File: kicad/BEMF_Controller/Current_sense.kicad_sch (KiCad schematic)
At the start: 24 parts, among them U13 INA181, U14 INA181, U15 INA181, U2 INA181

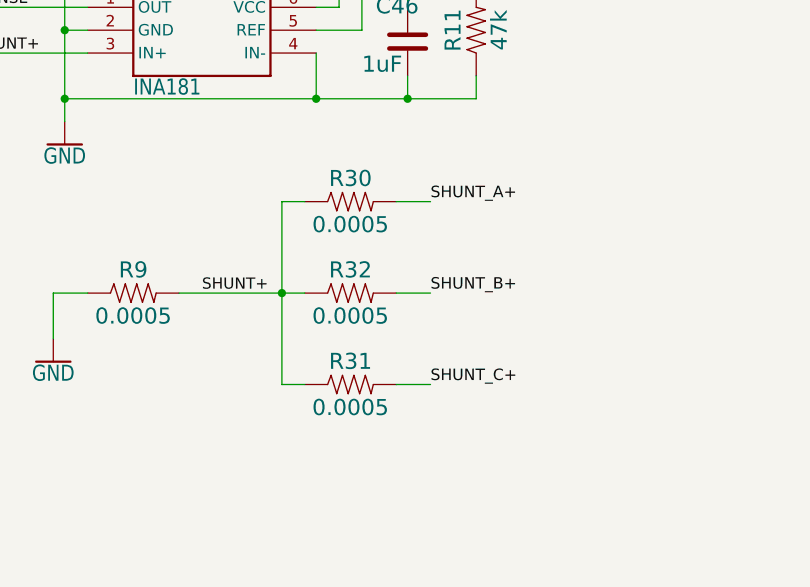
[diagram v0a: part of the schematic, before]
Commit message: Several updates to analog section
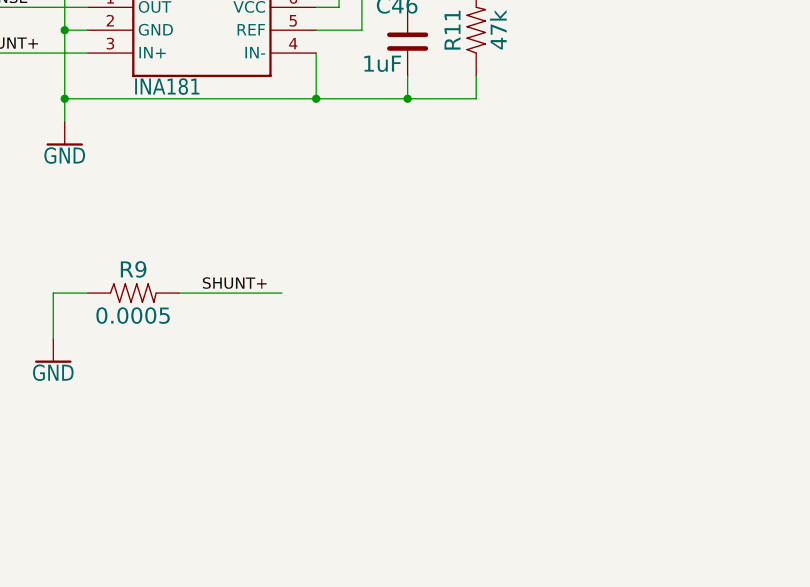
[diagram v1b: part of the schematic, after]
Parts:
- removed R30, R31, R32: 0.0005, main:R2512, symbol main-eagle-import:RESISTOR

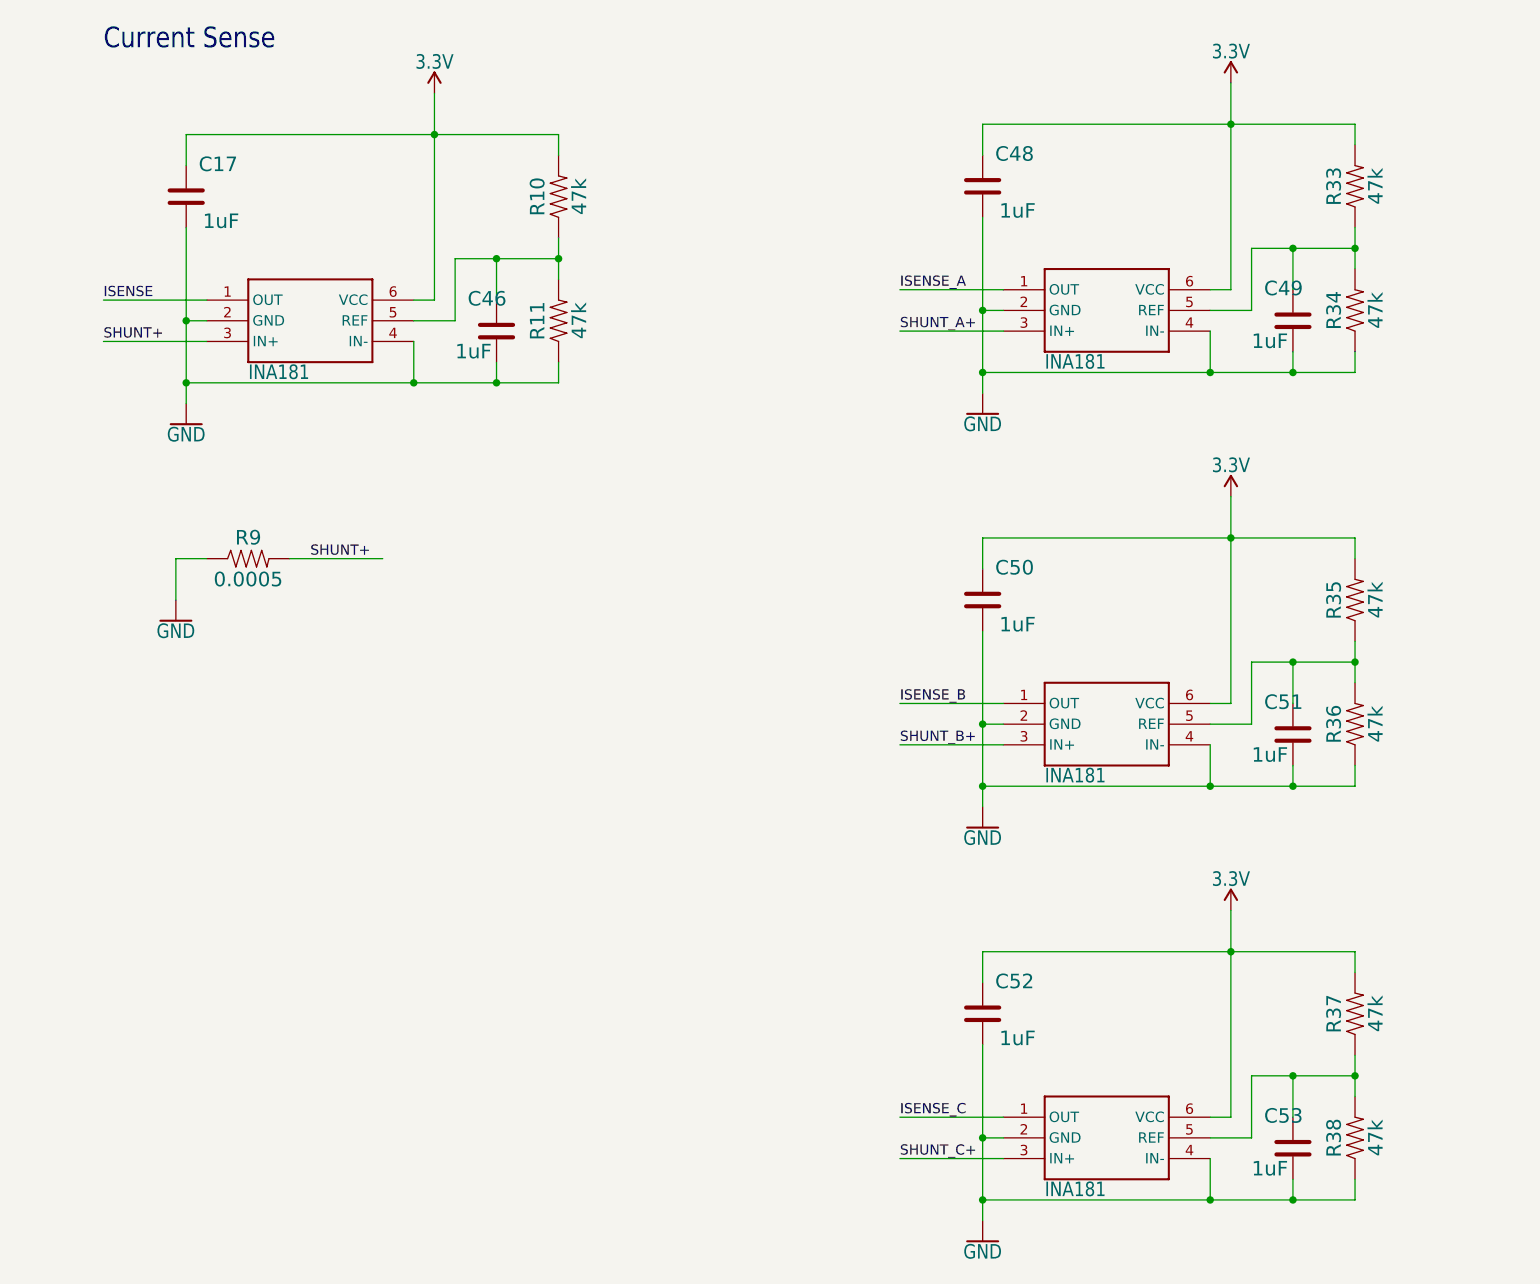
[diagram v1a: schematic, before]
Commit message: Further work on a/o current sensing circuits.
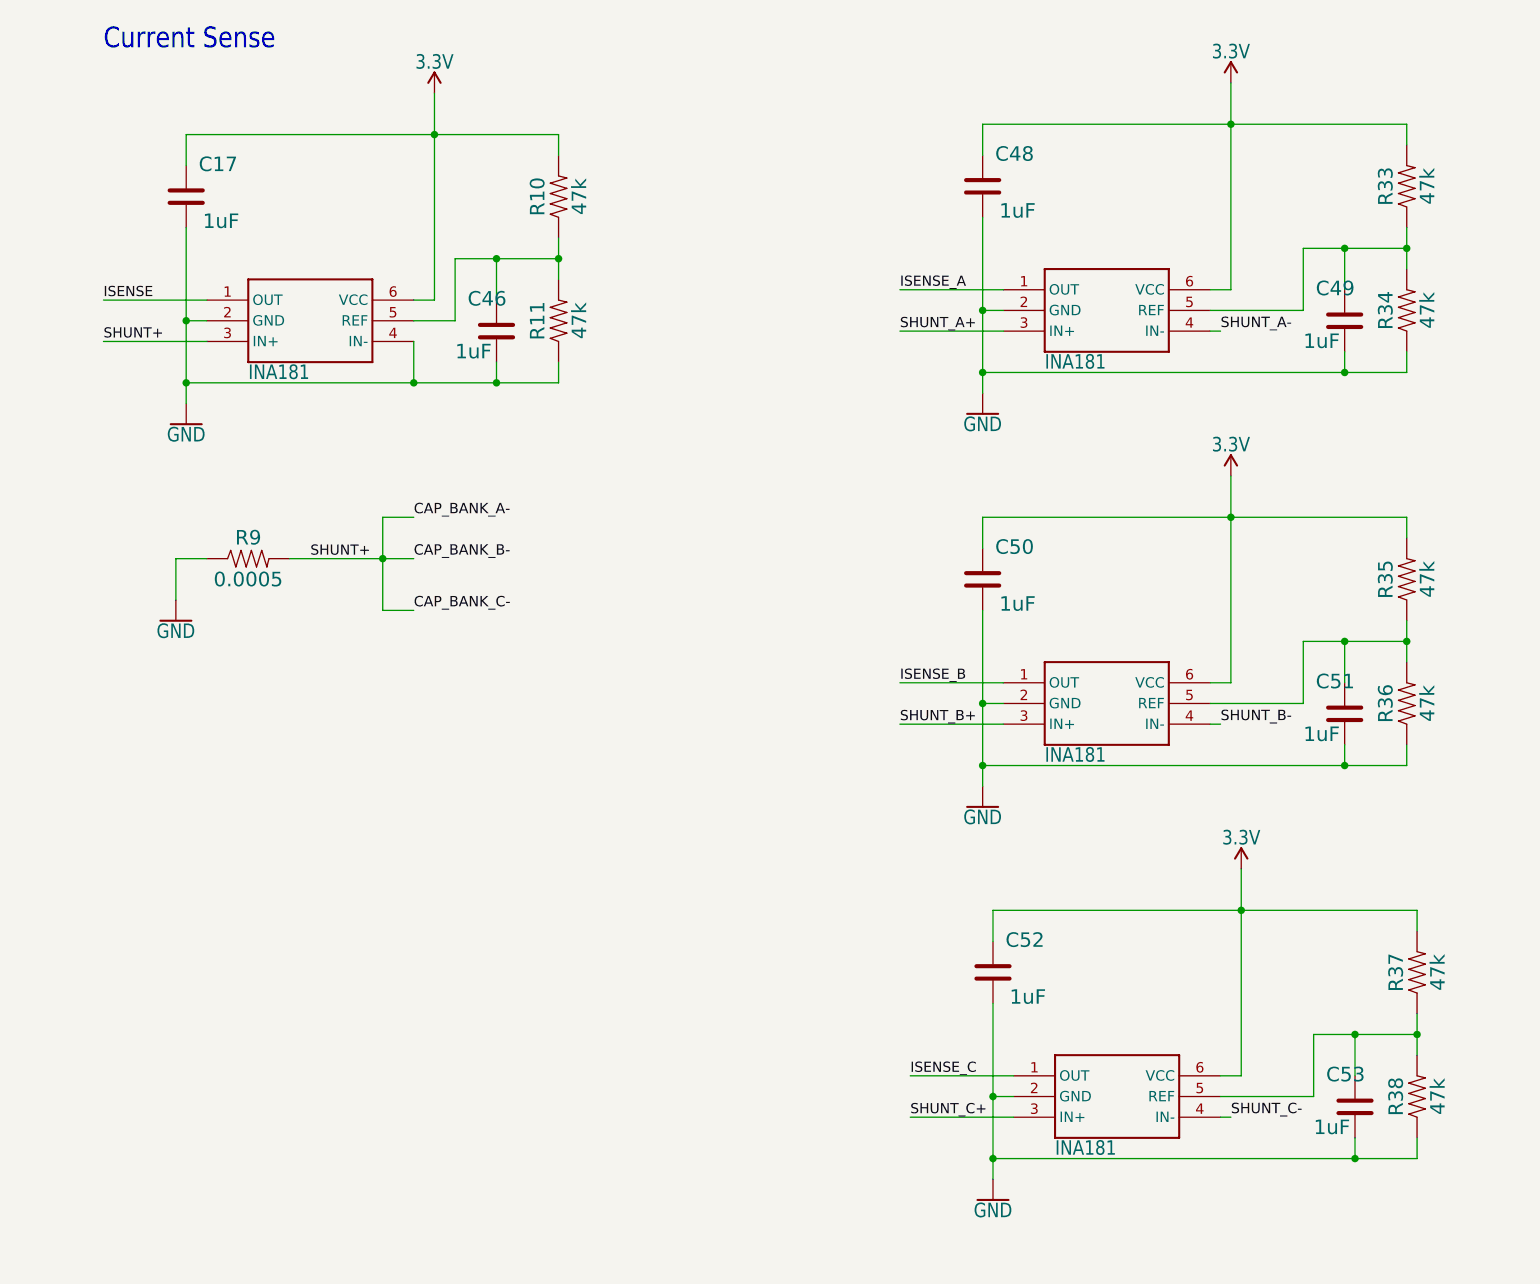
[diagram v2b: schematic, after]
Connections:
- net GND: no longer U13.4 (IN-), U14.4 (IN-), U15.4 (IN-)
- net SHUNT+ renamed CAP_BANK_A-
- new net SHUNT_A-: U13.4 (IN-)
- new net SHUNT_B-: U14.4 (IN-)
- new net SHUNT_C-: U15.4 (IN-)
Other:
- moved on the sheet: C49, R33, R34

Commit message: First version of PCB layout.
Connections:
- net GND: no longer C48.2, C49.2, C50.2, C51.2, C52.2, C53.2, R34.1, R36.1, R38.1, U13.2 (GND), U14.2 (GND), U15.2 (GND)
- net CAP_BANK_A- renamed CAP_BANK_GND
- net CAP_BANK_GND: now also C48.2, C49.2, C50.2, C51.2, C52.2, C53.2, R34.1, R36.1, R38.1, U13.2 (GND), U14.2 (GND), U15.2 (GND)
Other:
- moved on the sheet: C49, C51, C53, R33, R34, R35, R36, R37, R38

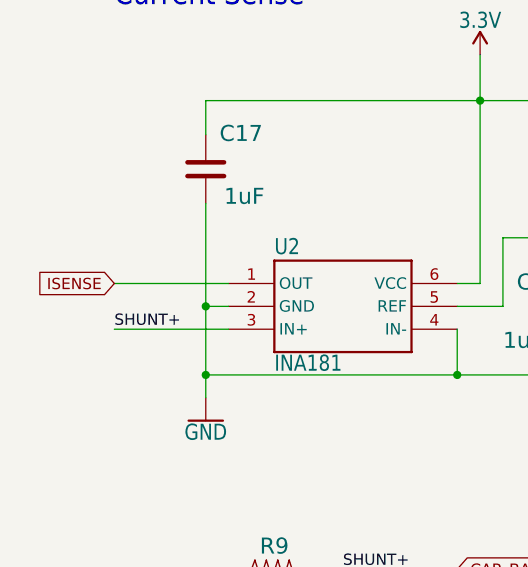
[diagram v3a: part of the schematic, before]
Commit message: Feature complete, zero eroors in pcb. Still lot of warnings.
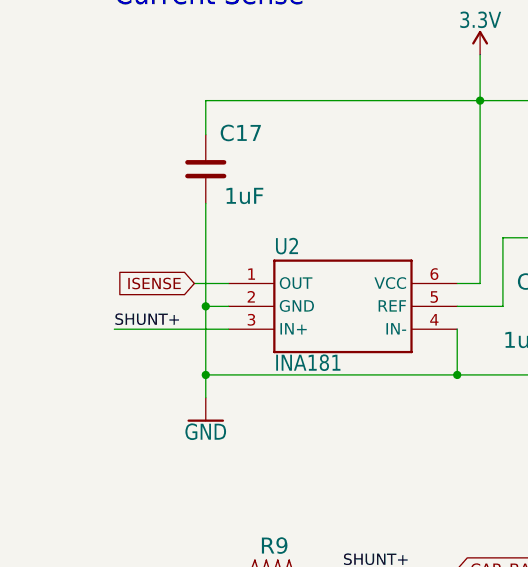
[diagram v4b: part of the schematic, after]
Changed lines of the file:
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@@
 	(wire
 		(pts
-			(xy 31.75 55.88) (xy 19.05 55.88)
+			(xy 31.75 55.88) (xy 27.94 55.88)
 		)
 		(stroke
@@
 	(global_label "ISENSE"
 		(shape input)
-		(at 19.05 55.88 180)
+		(at 27.94 55.88 180)
 		(fields_autoplaced yes)
 		(effects
@@
 		)
 		(property "Intersheetrefs" "${INTERSHEET_REFS}"
-			(at 9.6054 55.88 0)
+			(at 18.4954 55.88 0)
 			(effects
 				(font

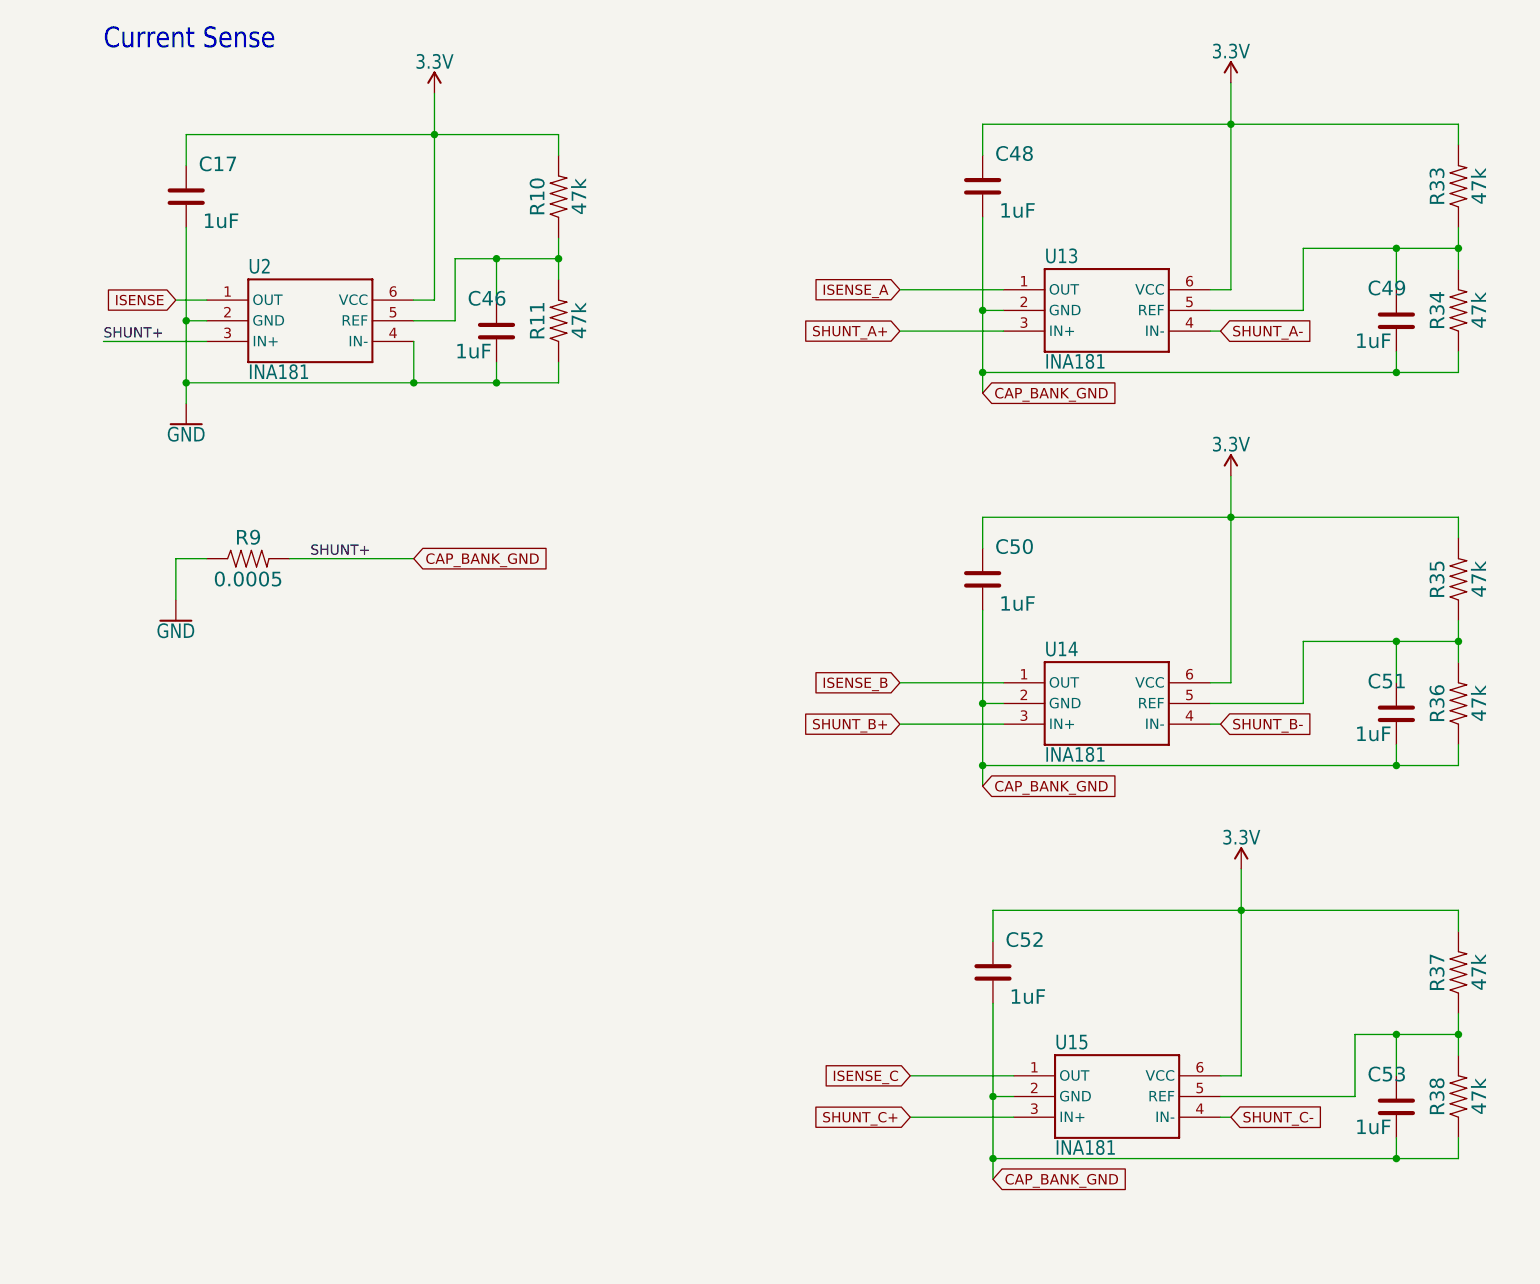
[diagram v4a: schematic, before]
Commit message: Fixed all warnings.
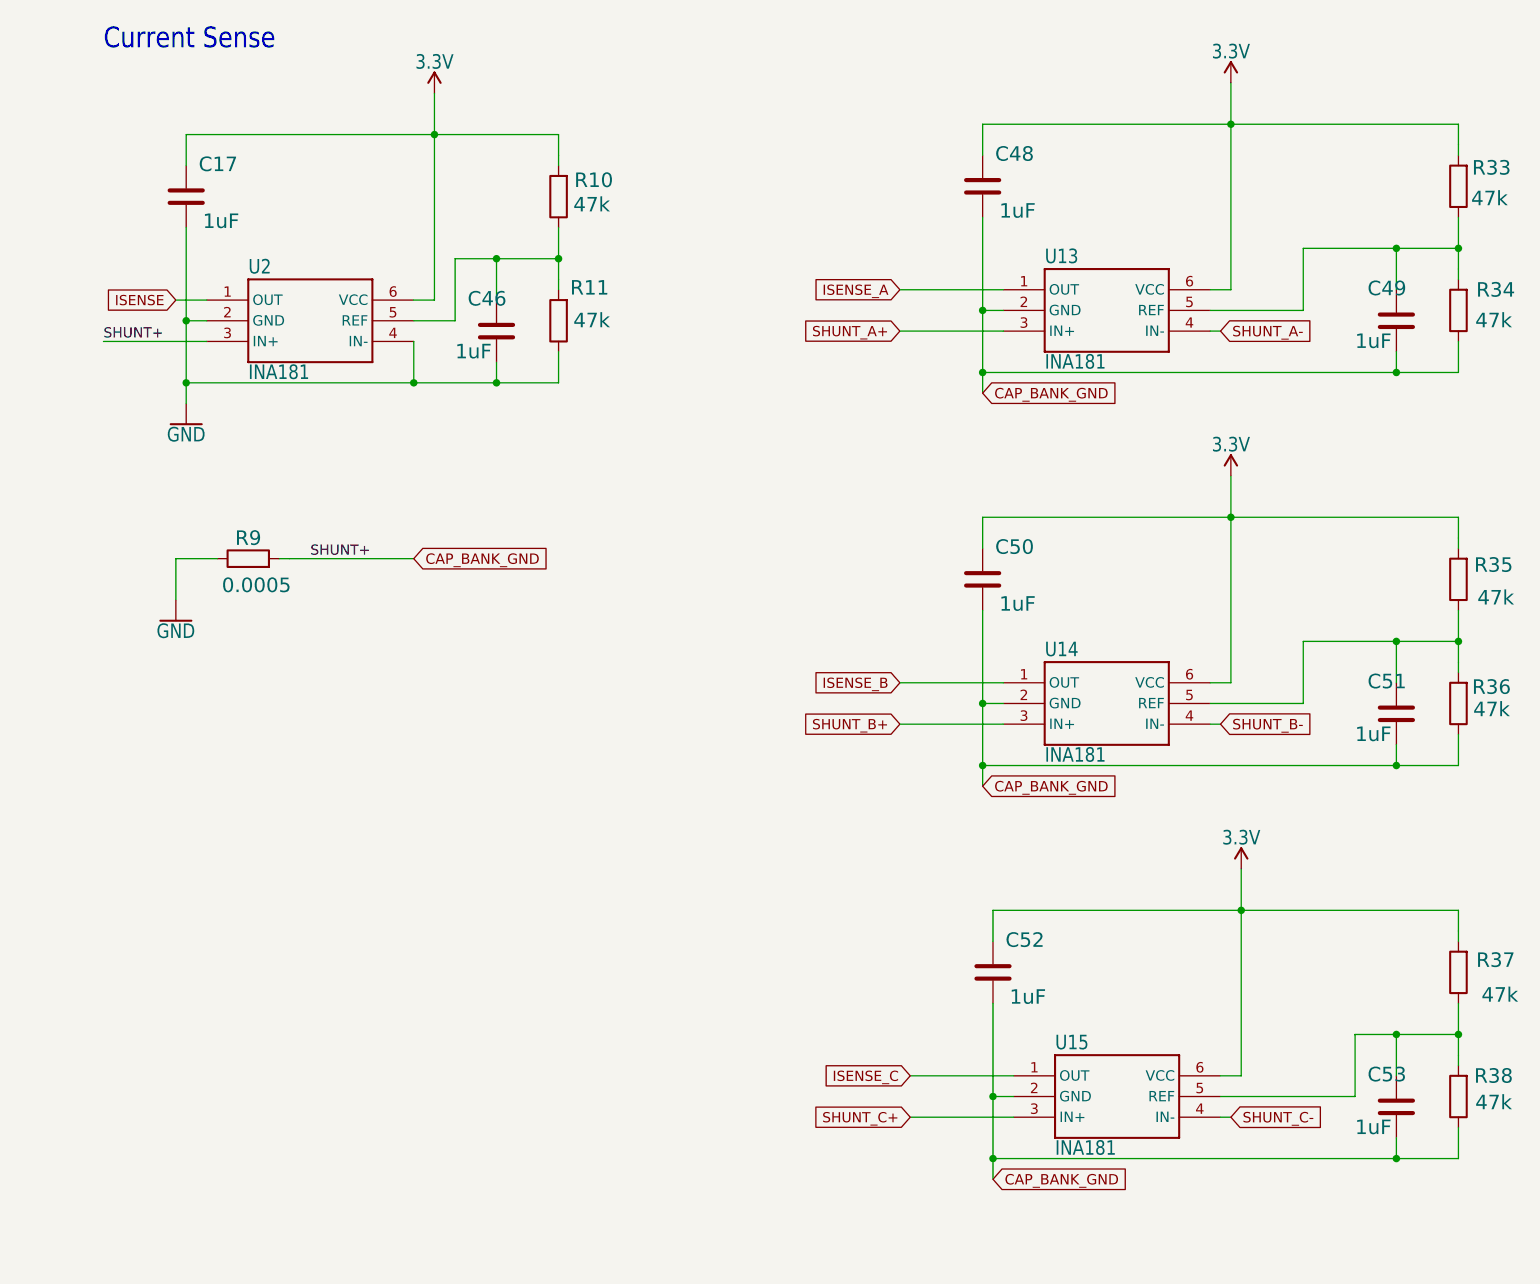
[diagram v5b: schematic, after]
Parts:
- R10, R11, R33, R34, R35, R36, R37, R38: footprint main:1206 -> Resistor_SMD:R_1206_3216Metric; symbol main-eagle-import:RESISTOR1206 -> Component_Library:R47k
- R9: footprint main:R2512 -> Resistor_SMD:R_2512_6332Metric_Pad1.40x3.35mm_HandSolder; symbol main-eagle-import:RESISTOR -> Component_Library:R0005
